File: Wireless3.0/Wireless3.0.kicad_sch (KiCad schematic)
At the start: 7 parts, among them J1 Serial 1, J2 Serial 2, J3 Serial 3, J4 Serial 4, J5 Serial 5, J6 Power, U1 ESP32-S3-DEVKITC-1-N8R2

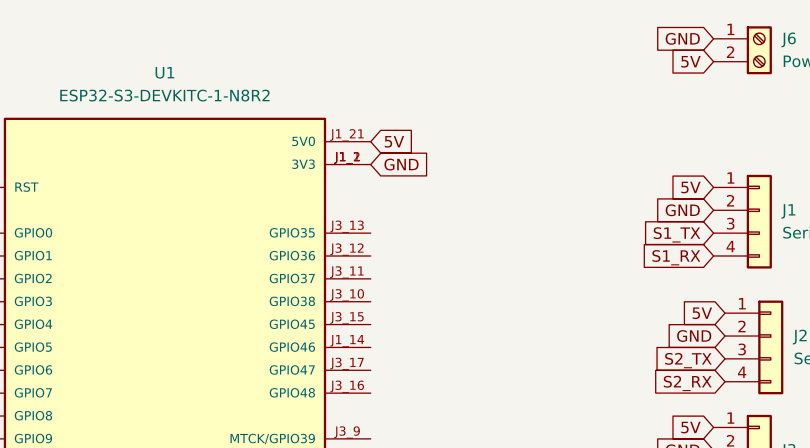
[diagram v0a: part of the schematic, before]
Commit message: updated wcb 3.0 to 3.1
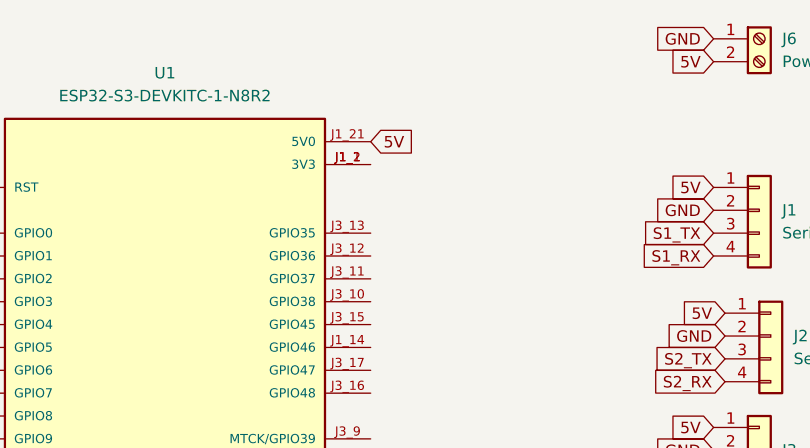
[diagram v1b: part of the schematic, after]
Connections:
- net GND: no longer U1.J1_1 (3V3), U1.J1_2 (3V3)
- new net: U1.J1_1 (3V3), U1.J1_2 (3V3)
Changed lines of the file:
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@@
-		)
-	)
-	(global_label "GND"
-		(shape input)
-		(at 90.17 41.91 0)
-		(fields_autoplaced yes)
-		(effects
-			(font
-				(size 1.27 1.27)
-			)
-			(justify left)
-		)
-		(property "Intersheetrefs" "${INTERSHEET_REFS}"
-			(at 97.0257 41.91 0)
-			(effects
-				(font
-					(size 1.27 1.27)
-				)
-				(justify left)
-				(hide yes)
-			)
 		)
 	)
